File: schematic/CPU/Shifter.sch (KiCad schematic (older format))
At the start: 10 parts, among them U19 74LS157, U20 74LS157, U21 74LS157, U22 74LS157, U23 74LS157, U24 74LS157, U25 74LS157, U26 74LS157, U27 74LS157, U28 74LS157

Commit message: schematic finished
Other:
- note added: "board 10"
- note added: "board 11\n"
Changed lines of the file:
@@
 Wire Wire Line
 	1900 5300 2150 5300
-Text Label 1950 1000 0    50   ~ 0
+Text Label 1150 600  0    50   ~ 0
 reverse
 Wire Wire Line
-	1950 1000 1800 1000
-Text HLabel 1800 1000 0    50   Input ~ 0
+	1150 600  1000 600
+Text HLabel 1000 600  0    50   Input ~ 0
 rightNotLeft
 $Comp
@@
 Wire Wire Line
 	6400 4400 6650 4400
-Text HLabel 1800 1150 0    50   Input ~ 0
+Text HLabel 1000 750  0    50   Input ~ 0
 b0
-Text HLabel 1800 1250 0    50   Input ~ 0
+Text HLabel 1000 850  0    50   Input ~ 0
 b1
-Text HLabel 1800 1350 0    50   Input ~ 0
+Text HLabel 1000 950  0    50   Input ~ 0
 b2
-Text Label 1950 1150 0    50   ~ 0
+Text Label 1150 750  0    50   ~ 0
 shift1
-Text Label 1950 1250 0    50   ~ 0
+Text Label 1150 850  0    50   ~ 0
 shift2
-Text Label 1950 1350 0    50   ~ 0
+Text Label 1150 950  0    50   ~ 0
 shift4
 Wire Wire Line
-	1800 1150 1950 1150
-Wire Wire Line
-	1800 1250 1950 1250
-Wire Wire Line
-	1950 1350 1800 1350
+	1000 750  1150 750
+Wire Wire Line
+	1000 850  1150 850
+Wire Wire Line
+	1150 950  1000 950
 Text Label 3500 3400 2    50   ~ 0
 shift1
@@
 	1    0    0    -1
 $EndComp
+Wire Notes Line width 12
+	3250 1200 3250 6400
+Wire Notes Line width 12
+	3250 6400 8200 6400
+Wire Notes Line width 12
+	8200 6400 8200 3950
+Wire Notes Line width 12
+	8200 3950 9600 3950
+Wire Notes Line width 12
+	9600 3950 9600 1200
+Wire Notes Line width 12
+	9600 1200 3250 1200
+Text Notes 3300 1400 0    100  ~ 20
+board 10
+Wire Notes Line
+	3600 2200 3250 2200
+Wire Notes Line
+	3250 2200 3250 1200
+Wire Notes Line width 12
+	3250 1200 1200 1200
+Wire Notes Line width 12
+	1200 1200 1200 6500
+Wire Notes Line width 12
+	1200 6500 9600 6500
+Wire Notes Line width 12
+	9600 6500 9600 3950
+Text Notes 1250 1400 0    100  ~ 20
+board 11\n
 $EndSCHEMATC

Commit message: schematic with henry
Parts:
- renumbered U19 to U13, U20 to U14, U21 to U15, U22 to U16, U23 to U17, U24 to U18, U25 to U19, U26 to U20, U27 to U21, U28 to U22
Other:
- note removed: "board 10"
- note removed: "board 11\n"
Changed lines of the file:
@@
 $Descr A4 11693 8268
 encoding utf-8
-Sheet 3 17
+Sheet 3 18
 Title ""
 Date ""
@@
 $EndDescr
 $Comp
-L 74xx:74LS157 U19
+L 74xx:74LS157 U13
 U 1 1 6029780F
 P 2650 2800
-F 0 "U19" H 2650 3881 50  0000 C CNN
+F 0 "U13" H 2650 3881 50  0000 C CNN
 F 1 "74LS157" H 2650 3790 50  0000 C CNN
 F 2 "Package_DIP:DIP-16_W7.62mm" H 2650 2800 50  0001 C CNN
@@
 $EndComp
 $Comp
-L 74xx:74LS157 U20
+L 74xx:74LS157 U14
 U 1 1 602993AB
 P 2650 5000
-F 0 "U20" H 2650 6081 50  0000 C CNN
-F 1 "74LS157" H 2650 5990 50  0000 C CNN
+F 0 "U14" H 2750 5850 50  0000 C CNN
+F 1 "74LS157" H 2900 5950 50  0000 C CNN
 F 2 "Package_DIP:DIP-16_W7.62mm" H 2650 5000 50  0001 C CNN
 F 3 "http://www.ti.com/lit/gpn/sn74LS157" H 2650 5000 50  0001 C CNN
@@
 P 2650 1900
 F 0 "#PWR046" H 2650 1750 50  0001 C CNN
-F 1 "+5V" H 2665 2073 50  0000 C CNN
+F 1 "+5V" H 2650 2200 50  0000 C CNN
 F 2 "" H 2650 1900 50  0001 C CNN
 F 3 "" H 2650 1900 50  0001 C CNN
@@
 rightNotLeft
 $Comp
-L 74xx:74LS157 U21
+L 74xx:74LS157 U15
 U 1 1 602A7A35
 P 4150 2800
-F 0 "U21" H 4150 3881 50  0000 C CNN
+F 0 "U15" H 4150 3881 50  0000 C CNN
 F 1 "74LS157" H 4150 3790 50  0000 C CNN
 F 2 "Package_DIP:DIP-16_W7.62mm" H 4150 2800 50  0001 C CNN
@@
 $EndComp
 $Comp
-L 74xx:74LS157 U22
+L 74xx:74LS157 U16
 U 1 1 602A7A3B
 P 4150 5000
-F 0 "U22" H 4150 6081 50  0000 C CNN
-F 1 "74LS157" H 4150 5990 50  0000 C CNN
+F 0 "U16" H 4250 5850 50  0000 C CNN
+F 1 "74LS157" H 4350 5950 50  0000 C CNN
 F 2 "Package_DIP:DIP-16_W7.62mm" H 4150 5000 50  0001 C CNN
 F 3 "http://www.ti.com/lit/gpn/sn74LS157" H 4150 5000 50  0001 C CNN
@@
 P 4150 1900
 F 0 "#PWR053" H 4150 1750 50  0001 C CNN
-F 1 "+5V" H 4165 2073 50  0000 C CNN
+F 1 "+5V" H 4150 2200 50  0000 C CNN
 F 2 "" H 4150 1900 50  0001 C CNN
 F 3 "" H 4150 1900 50  0001 C CNN
@@
 	3550 2500 3150 2500
 $Comp
-L 74xx:74LS157 U23
+L 74xx:74LS157 U17
 U 1 1 602B6E77
 P 5650 2800
-F 0 "U23" H 5650 3881 50  0000 C CNN
+F 0 "U17" H 5650 3881 50  0000 C CNN
 F 1 "74LS157" H 5650 3790 50  0000 C CNN
 F 2 "Package_DIP:DIP-16_W7.62mm" H 5650 2800 50  0001 C CNN
@@
 $EndComp
 $Comp
-L 74xx:74LS157 U24
+L 74xx:74LS157 U18
 U 1 1 602B6E7D
 P 5650 5000
-F 0 "U24" H 5650 6081 50  0000 C CNN
-F 1 "74LS157" H 5650 5990 50  0000 C CNN
+F 0 "U18" H 5750 5850 50  0000 C CNN
+F 1 "74LS157" H 5900 5950 50  0000 C CNN
 F 2 "Package_DIP:DIP-16_W7.62mm" H 5650 5000 50  0001 C CNN
 F 3 "http://www.ti.com/lit/gpn/sn74LS157" H 5650 5000 50  0001 C CNN
@@
 P 5650 1900
 F 0 "#PWR061" H 5650 1750 50  0001 C CNN
-F 1 "+5V" H 5665 2073 50  0000 C CNN
+F 1 "+5V" H 5650 2150 50  0000 C CNN
 F 2 "" H 5650 1900 50  0001 C CNN
 F 3 "" H 5650 1900 50  0001 C CNN
@@
 Shift2 MUXs
 $Comp
-L 74xx:74LS157 U25
+L 74xx:74LS157 U19
 U 1 1 602DB8CC
 P 7150 2800
-F 0 "U25" H 7150 3881 50  0000 C CNN
+F 0 "U19" H 7150 3881 50  0000 C CNN
 F 1 "74LS157" H 7150 3790 50  0000 C CNN
 F 2 "Package_DIP:DIP-16_W7.62mm" H 7150 2800 50  0001 C CNN
@@
 $EndComp
 $Comp
-L 74xx:74LS157 U26
+L 74xx:74LS157 U20
 U 1 1 602DB8D2
 P 7150 5000
-F 0 "U26" H 7150 6081 50  0000 C CNN
-F 1 "74LS157" H 7150 5990 50  0000 C CNN
+F 0 "U20" H 7250 5850 50  0000 C CNN
+F 1 "74LS157" H 7400 5950 50  0000 C CNN
 F 2 "Package_DIP:DIP-16_W7.62mm" H 7150 5000 50  0001 C CNN
 F 3 "http://www.ti.com/lit/gpn/sn74LS157" H 7150 5000 50  0001 C CNN
@@
 P 7150 1900
 F 0 "#PWR071" H 7150 1750 50  0001 C CNN
-F 1 "+5V" H 7165 2073 50  0000 C CNN
+F 1 "+5V" H 7150 2150 50  0000 C CNN
 F 2 "" H 7150 1900 50  0001 C CNN
 F 3 "" H 7150 1900 50  0001 C CNN
@@
 	6350 3400 6650 3400
 $Comp
-L 74xx:74LS157 U27
+L 74xx:74LS157 U21
 U 1 1 6032FFD0
 P 8800 2800
-F 0 "U27" H 8800 3881 50  0000 C CNN
+F 0 "U21" H 8800 3881 50  0000 C CNN
 F 1 "74LS157" H 8800 3790 50  0000 C CNN
 F 2 "Package_DIP:DIP-16_W7.62mm" H 8800 2800 50  0001 C CNN
@@
 $EndComp
 $Comp
-L 74xx:74LS157 U28
+L 74xx:74LS157 U22
 U 1 1 6032FFD6
 P 8800 5000
-F 0 "U28" H 8800 6081 50  0000 C CNN
-F 1 "74LS157" H 8800 5990 50  0000 C CNN
+F 0 "U22" H 8900 5850 50  0000 C CNN
+F 1 "74LS157" H 9050 5950 50  0000 C CNN
 F 2 "Package_DIP:DIP-16_W7.62mm" H 8800 5000 50  0001 C CNN
 F 3 "http://www.ti.com/lit/gpn/sn74LS157" H 8800 5000 50  0001 C CNN
@@
 $EndComp
 $Comp
-L power:GND #PWR079
+L power:GND #PWR080
 U 1 1 6032FFDC
 P 8800 6000
-F 0 "#PWR079" H 8800 5750 50  0001 C CNN
+F 0 "#PWR080" H 8800 5750 50  0001 C CNN
 F 1 "GND" H 8805 5827 50  0000 C CNN
 F 2 "" H 8800 6000 50  0001 C CNN
@@
 $EndComp
 $Comp
-L power:GND #PWR077
+L power:GND #PWR078
 U 1 1 6032FFE8
 P 8800 3800
-F 0 "#PWR077" H 8800 3550 50  0001 C CNN
+F 0 "#PWR078" H 8800 3550 50  0001 C CNN
 F 1 "GND" H 8805 3627 50  0000 C CNN
 F 2 "" H 8800 3800 50  0001 C CNN
@@
 $EndComp
 $Comp
-L power:+5V #PWR078
+L power:+5V #PWR079
 U 1 1 6032FFF4
 P 8800 4100
-F 0 "#PWR078" H 8800 3950 50  0001 C CNN
+F 0 "#PWR079" H 8800 3950 50  0001 C CNN
 F 1 "+5V" H 8815 4273 50  0000 C CNN
 F 2 "" H 8800 4100 50  0001 C CNN
@@
 	7650 5300 8050 5300
 $Comp
-L power:+5V #PWR0108
+L power:+5V #PWR077
 U 1 1 6032FB0C
 P 8800 1900
-F 0 "#PWR0108" H 8800 1750 50  0001 C CNN
-F 1 "+5V" H 8815 2073 50  0000 C CNN
+F 0 "#PWR077" H 8800 1750 50  0001 C CNN
+F 1 "+5V" H 8800 2150 50  0000 C CNN
 F 2 "" H 8800 1900 50  0001 C CNN
 F 3 "" H 8800 1900 50  0001 C CNN
@@
 	1    0    0    -1
 $EndComp
-Wire Notes Line width 12
-	3250 1200 3250 6400
-Wire Notes Line width 12
-	3250 6400 8200 6400
-Wire Notes Line width 12
-	8200 6400 8200 3950
-Wire Notes Line width 12
-	8200 3950 9600 3950
-Wire Notes Line width 12
-	9600 3950 9600 1200
-Wire Notes Line width 12
-	9600 1200 3250 1200
-Text Notes 3300 1400 0    100  ~ 20
-board 10
 Wire Notes Line
 	3600 2200 3250 2200
-Wire Notes Line
-	3250 2200 3250 1200
-Wire Notes Line width 12
-	3250 1200 1200 1200
-Wire Notes Line width 12
-	1200 1200 1200 6500
-Wire Notes Line width 12
-	1200 6500 9600 6500
-Wire Notes Line width 12
-	9600 6500 9600 3950
-Text Notes 1250 1400 0    100  ~ 20
-board 11\n
 $EndSCHEMATC

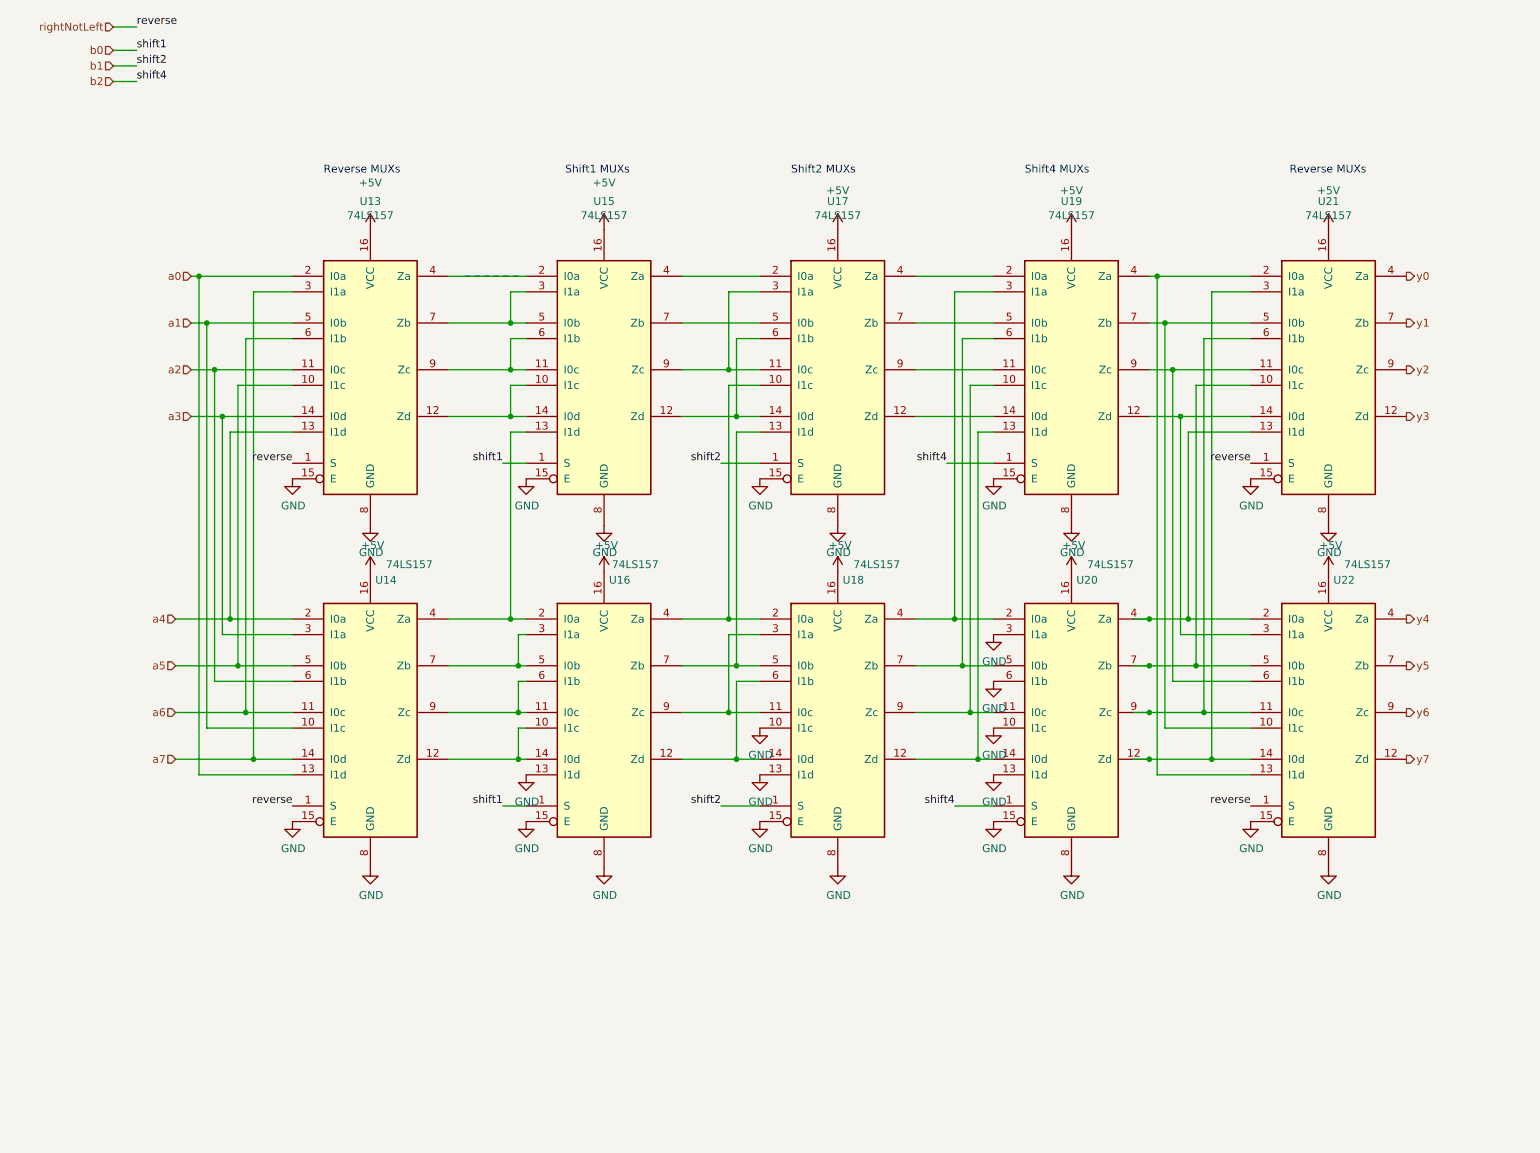
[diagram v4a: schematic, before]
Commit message: schematic: alu/shifter carry fix
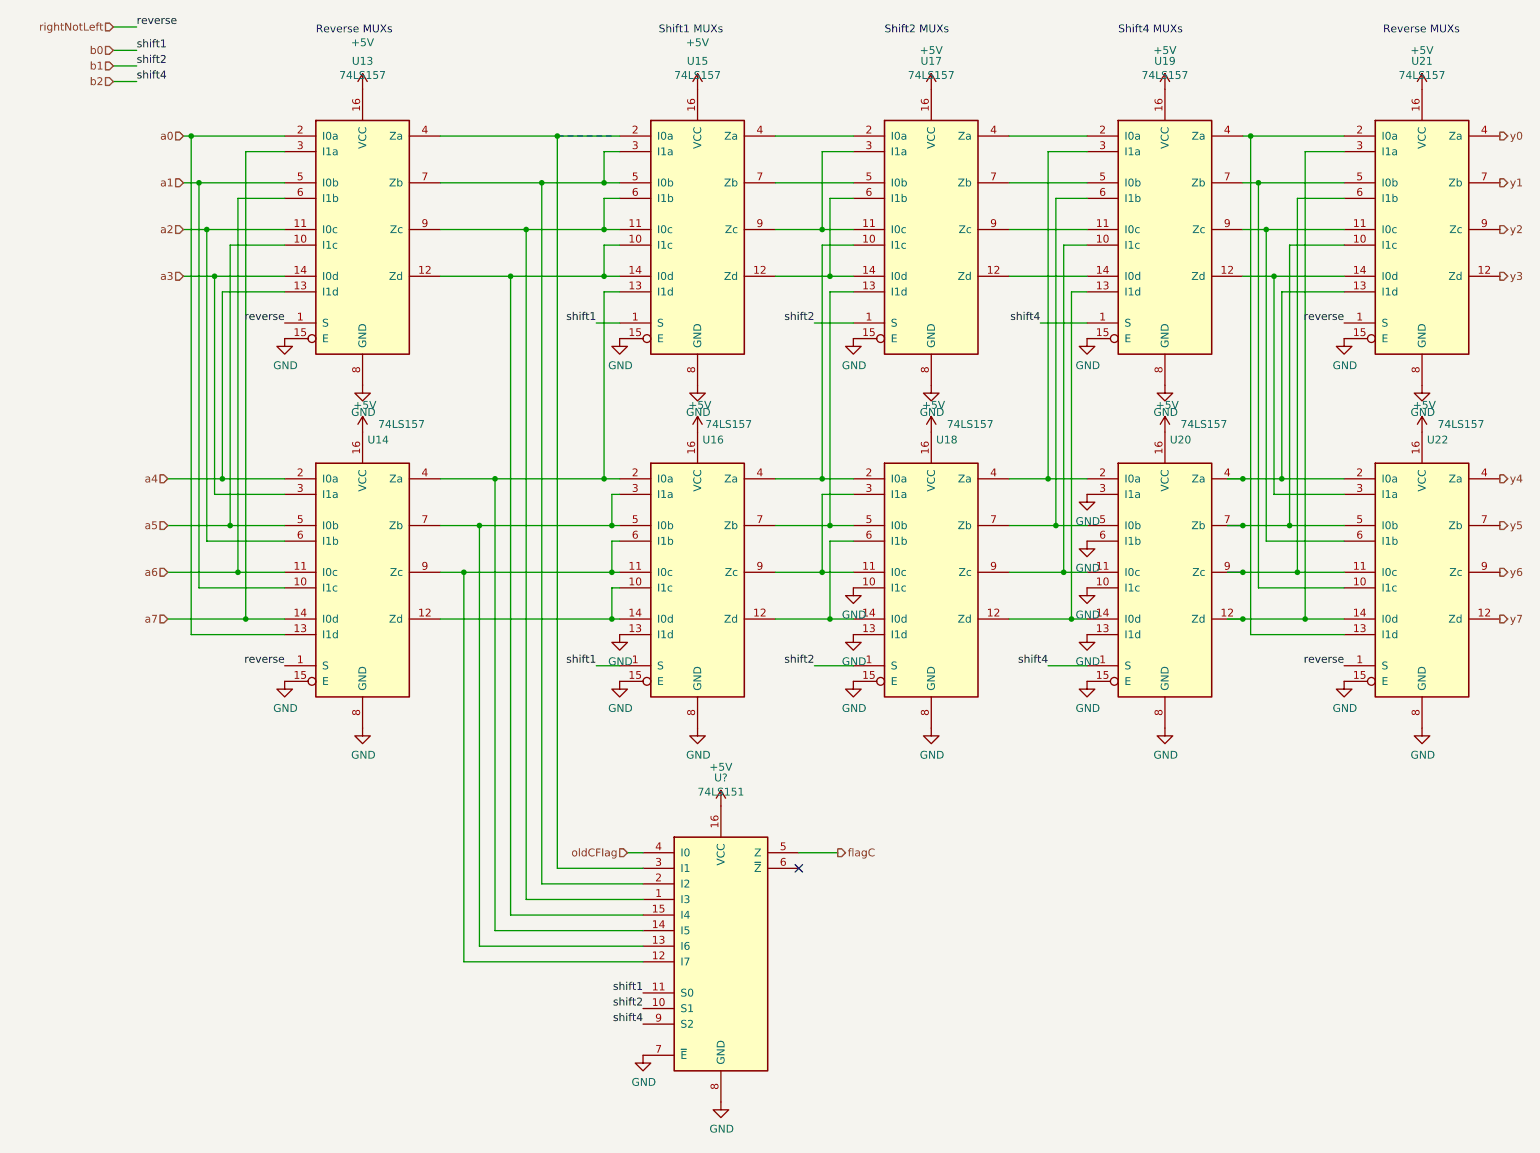
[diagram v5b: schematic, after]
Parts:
- added U?: 74LS151, symbol 74xx:74LS151
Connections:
- net +5V: now also U?.16 (VCC)
- net GND: now also U?.7 (~E), U?.8 (GND)
- net b0: now also U?.11 (S0)
- net b1: now also U?.10 (S1)
- net b2: now also U?.9 (S2)
- net at U13.12 (Zd), U15.10 (I1c), U15.14 (I0d): now also U?.15 (I4)
- net at U13.4 (Za), U15.2 (I0a): now also U?.3 (I1)
- net at U13.7 (Zb), U15.3 (I1a), U15.5 (I0b): now also U?.2 (I2)
- net at U13.9 (Zc), U15.11 (I0c), U15.6 (I1b): now also U?.1 (I3)
- net at U14.4 (Za), U15.13 (I1d), U16.2 (I0a): now also U?.14 (I5)
- net at U14.7 (Zb), U16.3 (I1a), U16.5 (I0b): now also U?.13 (I6)
- net at U14.9 (Zc), U16.11 (I0c), U16.6 (I1b): now also U?.12 (I7)
- new net flagC: U?.5 (Z)
- new net oldCFlag: U?.4 (I0)
- no-connect marks 0 -> 1
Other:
- moved on the sheet: U13, U14, U15, U16, U17, U18, U19, U20, U21, U22

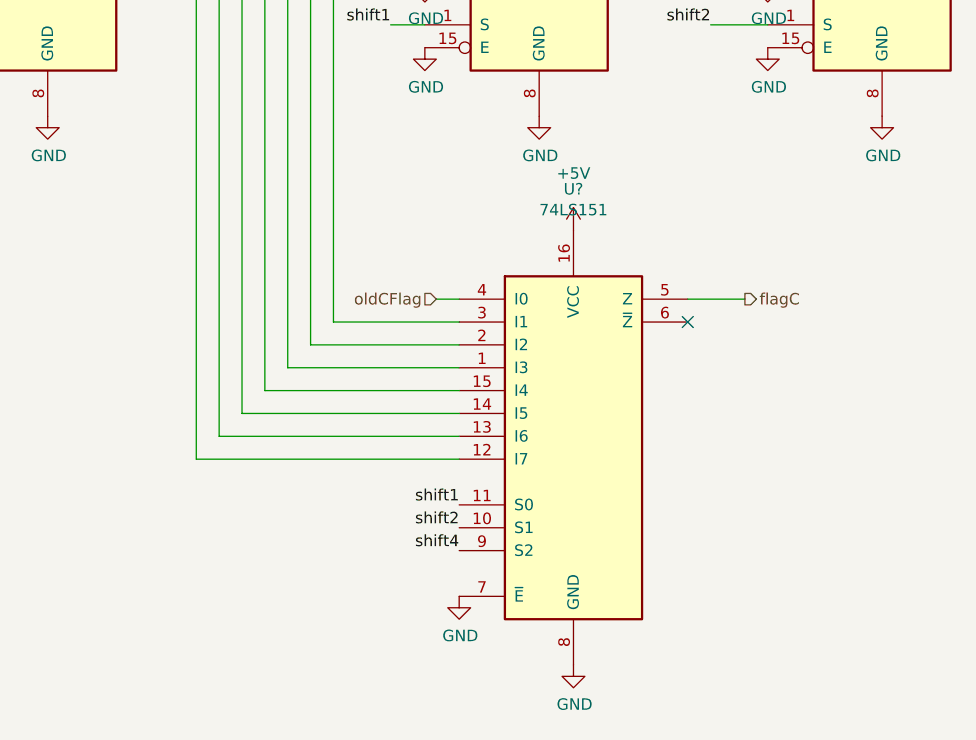
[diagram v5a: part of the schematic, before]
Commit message: fixed uart_rx and snake
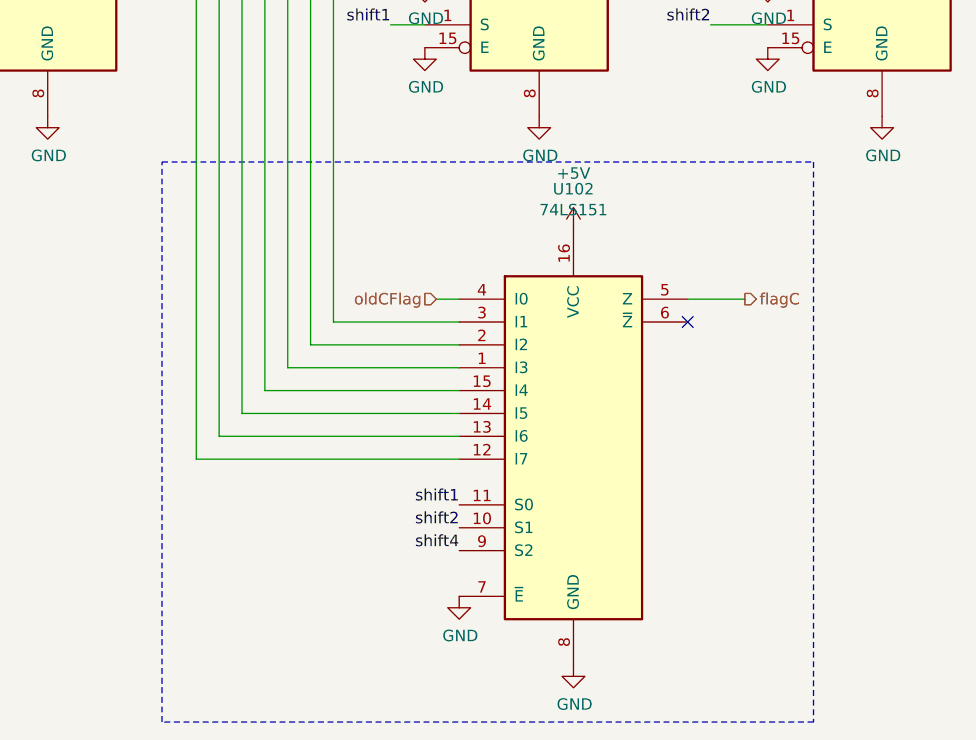
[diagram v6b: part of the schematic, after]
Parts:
- gave numbers to parts that had none: 1
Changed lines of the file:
@@
 AR Path="/608A8AE7/61BE49F5" Ref="#PWR?"  Part="1"
 AR Path="/600C5001/61BE49F5" Ref="#PWR?"  Part="1"
-F 0 "#PWR?" H 4900 7250 50  0001 C CNN
+AR Path="/600C5001/60297135/61BE49F5" Ref="#PWR0329"  Part="1"
+F 0 "#PWR0329" H 4900 7250 50  0001 C CNN
 F 1 "GND" H 4905 7327 50  0000 C CNN
 F 2 "" H 4900 7500 50  0001 C CNN
@@
 AR Path="/608A8AE7/61BE49FB" Ref="#PWR?"  Part="1"
 AR Path="/600C5001/61BE49FB" Ref="#PWR?"  Part="1"
-F 0 "#PWR?" H 4900 5450 50  0001 C CNN
+AR Path="/600C5001/60297135/61BE49FB" Ref="#PWR0328"  Part="1"
+F 0 "#PWR0328" H 4900 5450 50  0001 C CNN
 F 1 "+5V" H 4900 5850 50  0000 C CNN
 F 2 "" H 4900 5600 50  0001 C CNN
@@
 AR Path="/608A8AE7/61BE4A01" Ref="U?"  Part="1"
 AR Path="/600C5001/61BE4A01" Ref="U?"  Part="1"
-F 0 "U?" H 4900 7581 50  0000 C CNN
+AR Path="/600C5001/60297135/61BE4A01" Ref="U102"  Part="1"
+F 0 "U102" H 4900 7581 50  0000 C CNN
 F 1 "74LS151" H 4900 7490 50  0000 C CNN
 F 2 "" H 4900 6500 50  0001 C CNN
@@
 AR Path="/608A8AE7/61BE4A07" Ref="#PWR?"  Part="1"
 AR Path="/600C5001/61BE4A07" Ref="#PWR?"  Part="1"
-F 0 "#PWR?" H 4400 6950 50  0001 C CNN
+AR Path="/600C5001/60297135/61BE4A07" Ref="#PWR0327"  Part="1"
+F 0 "#PWR0327" H 4400 6950 50  0001 C CNN
 F 1 "GND" H 4405 7027 50  0000 C CNN
 F 2 "" H 4400 7200 50  0001 C CNN
@@
 Wire Wire Line
 	3250 4100 4200 4100
+Wire Notes Line rgb(255, 0, 0)
+	3100 5300 5950 5300
+Wire Notes Line rgb(255, 0, 0)
+	5950 5300 5950 7750
+Wire Notes Line rgb(255, 0, 0)
+	5950 7750 3100 7750
+Wire Notes Line rgb(255, 0, 0)
+	3100 7750 3100 5300
 $EndSCHEMATC
